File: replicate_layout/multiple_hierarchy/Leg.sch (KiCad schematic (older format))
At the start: 1 part, among them J201 LEG_out

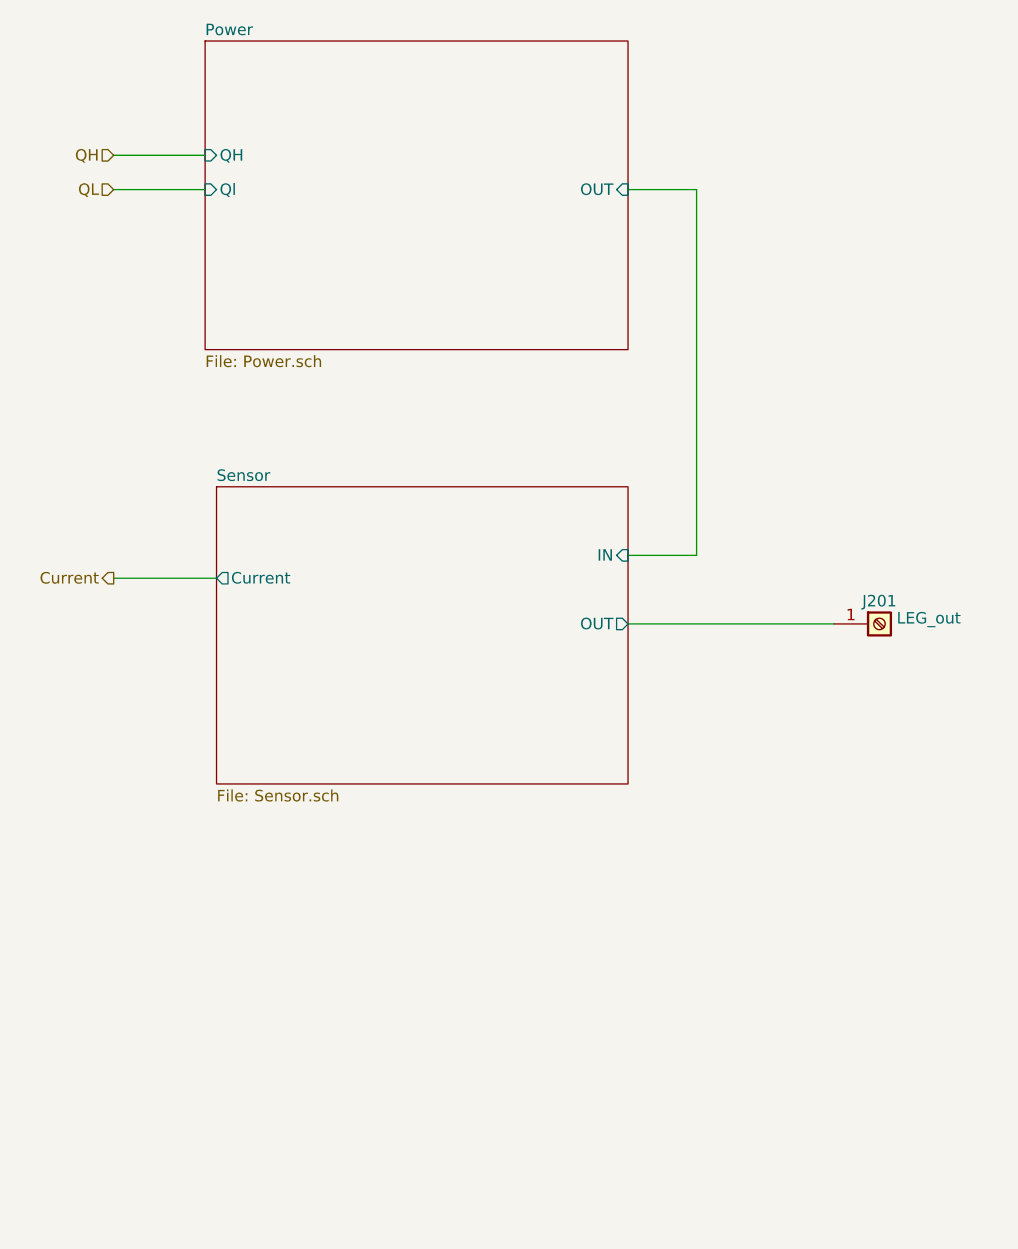
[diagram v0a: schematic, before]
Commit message: Changed test project to include complex hierarchy
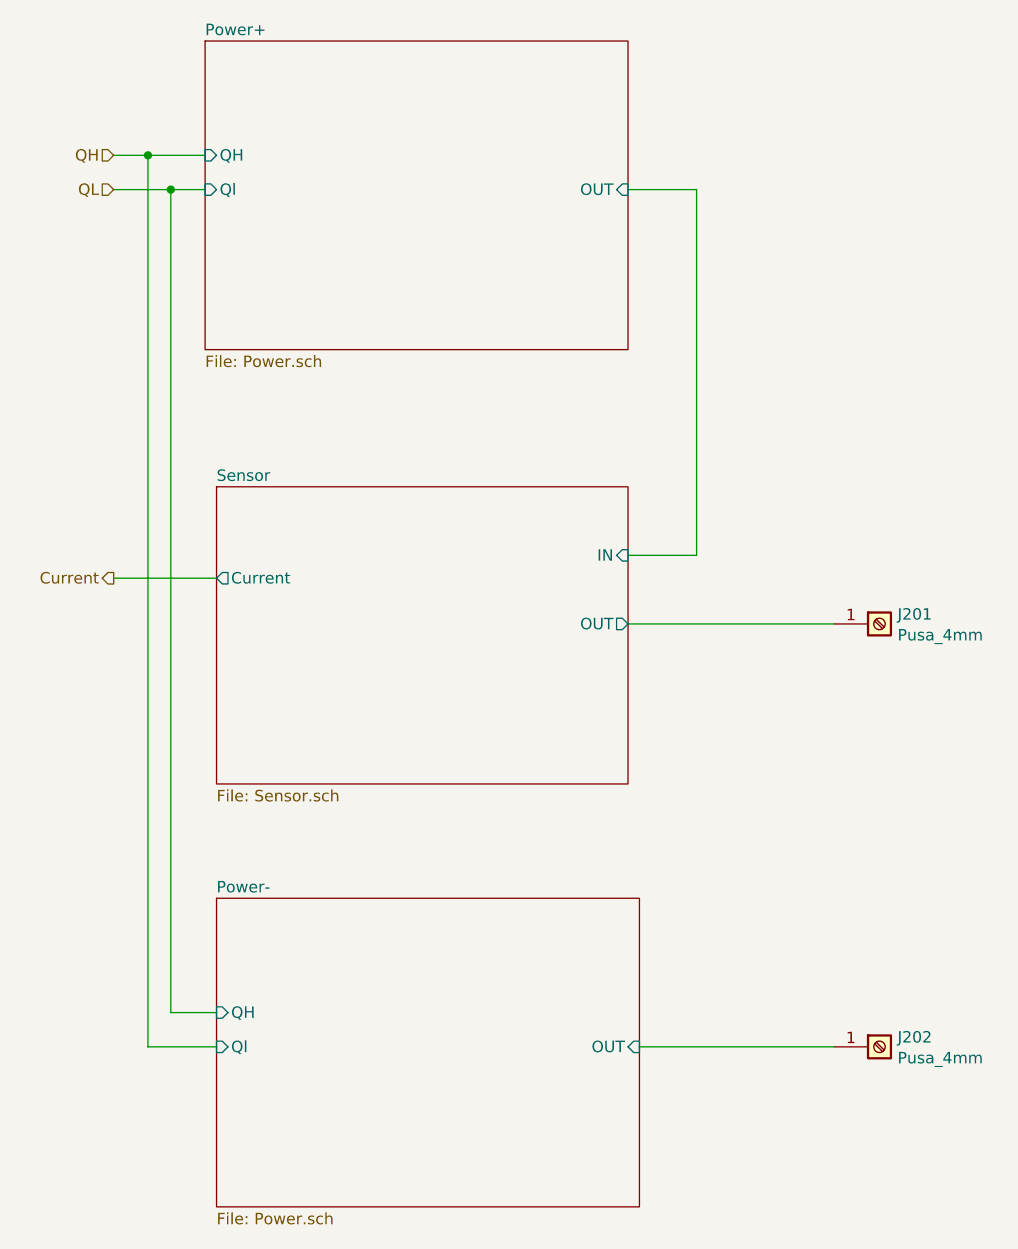
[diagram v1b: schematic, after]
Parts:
- added J202: Pusa_4mm, Connector:Pusa_4mm, symbol Connector:Pusa_4mm
- J201: value LEG_out -> Pusa_4mm
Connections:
- new net Power-/OUT: J202.1 (Pin_1)
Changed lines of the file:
@@
 $Descr A4 11693 8268
 encoding utf-8
-Sheet 2 10
+Sheet 2 13
 Title ""
 Date ""
@@
 S 4100 1450 1850 1350
 U 5B767FF2
-F0 "Power" 50
+F0 "Power+" 50
 F1 "Power.sch" 50
 F2 "OUT" I R 5950 2100 50
@@
 Wire Wire Line
 	5950 4000 6850 4000
-$Comp
-L Connector:Pusa_4mm J201
-U 1 1 5B76CB38
-P 7050 4000
-AR Path="/5B767FE4/5B76CB38" Ref="J201"  Part="1"
-AR Path="/5B76D023/5B76CB38" Ref="J501"  Part="1"
-AR Path="/5B76D031/5B76CB38" Ref="J801"  Part="1"
-F 0 "J201" H 7050 4100 50  0000 C CNN
-F 1 "LEG_out" H 7125 4025 50  0000 L CNN
-F 2 "Connector:Pusa_4mm" H 7125 3950 50  0001 L CNN
-F 3 "~" H 7050 4000 50  0001 C CNN
-	1    7050 4000
-	1    0    0    -1
-$EndComp
 Text HLabel 3700 1950 0    50   Input ~ 0
 QH
@@
 Current
 Wire Wire Line
-	3700 1950 4100 1950
+	3700 1950 3850 1950
 Wire Wire Line
-	4100 2100 3700 2100
+	4100 2100 3950 2100
 Wire Wire Line
 	3700 3800 4150 3800
+$Sheet
+S 4150 5200 1850 1350
+U 5B772791
+F0 "Power-" 50
+F1 "Power.sch" 50
+F2 "OUT" I R 6000 5850 50
+F3 "QH" I L 4150 5700 50
+F4 "Ql" I L 4150 5850 50
+$EndSheet
+Wire Wire Line
+	4150 5700 3950 5700
+Wire Wire Line
+	3950 5700 3950 2100
+Connection ~ 3950 2100
+Wire Wire Line
+	3950 2100 3700 2100
+Wire Wire Line
+	3850 1950 3850 5850
+Wire Wire Line
+	3850 5850 4150 5850
+Connection ~ 3850 1950
+Wire Wire Line
+	3850 1950 4100 1950
+Wire Wire Line
+	6000 5850 6850 5850
+$Comp
+L Connector:Pusa_4mm J201
+U 1 1 5B772913
+P 7050 4000
+AR Path="/5B767FE4/5B772913" Ref="J201"  Part="1"
+AR Path="/5B76D023/5B772913" Ref="J601"  Part="1"
+AR Path="/5B76D031/5B772913" Ref="J1001"  Part="1"
+F 0 "J201" H 7129 4042 50  0000 L CNN
+F 1 "Pusa_4mm" H 7129 3951 50  0000 L CNN
+F 2 "Connector:Pusa_4mm" H 7125 3950 50  0001 L CNN
+F 3 "~" H 7050 4000 50  0001 C CNN
+	1    7050 4000
+	1    0    0    -1
+$EndComp
+$Comp
+L Connector:Pusa_4mm J202
+U 1 1 5B77299E
+P 7050 5850
+AR Path="/5B767FE4/5B77299E" Ref="J202"  Part="1"
+AR Path="/5B76D023/5B77299E" Ref="J602"  Part="1"
+AR Path="/5B76D031/5B77299E" Ref="J1002"  Part="1"
+F 0 "J202" H 7129 5892 50  0000 L CNN
+F 1 "Pusa_4mm" H 7129 5801 50  0000 L CNN
+F 2 "Connector:Pusa_4mm" H 7125 5800 50  0001 L CNN
+F 3 "~" H 7050 5850 50  0001 C CNN
+	1    7050 5850
+	1    0    0    -1
+$EndComp
 $EndSCHEMATC
